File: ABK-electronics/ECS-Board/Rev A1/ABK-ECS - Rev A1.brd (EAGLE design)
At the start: 80 x 80 mm, 141 parts, among them J1 1241050-5, J2 USB3075-30-A, J3 22-27-2061-06, J4 22-05-7068-06, J5 22-05-7028-02, J6 22-05-7028-02, J7 22-05-7068-06, K3 G6K-2G-Y, SW1 B3FS-1015, SW2 B3FS-1015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

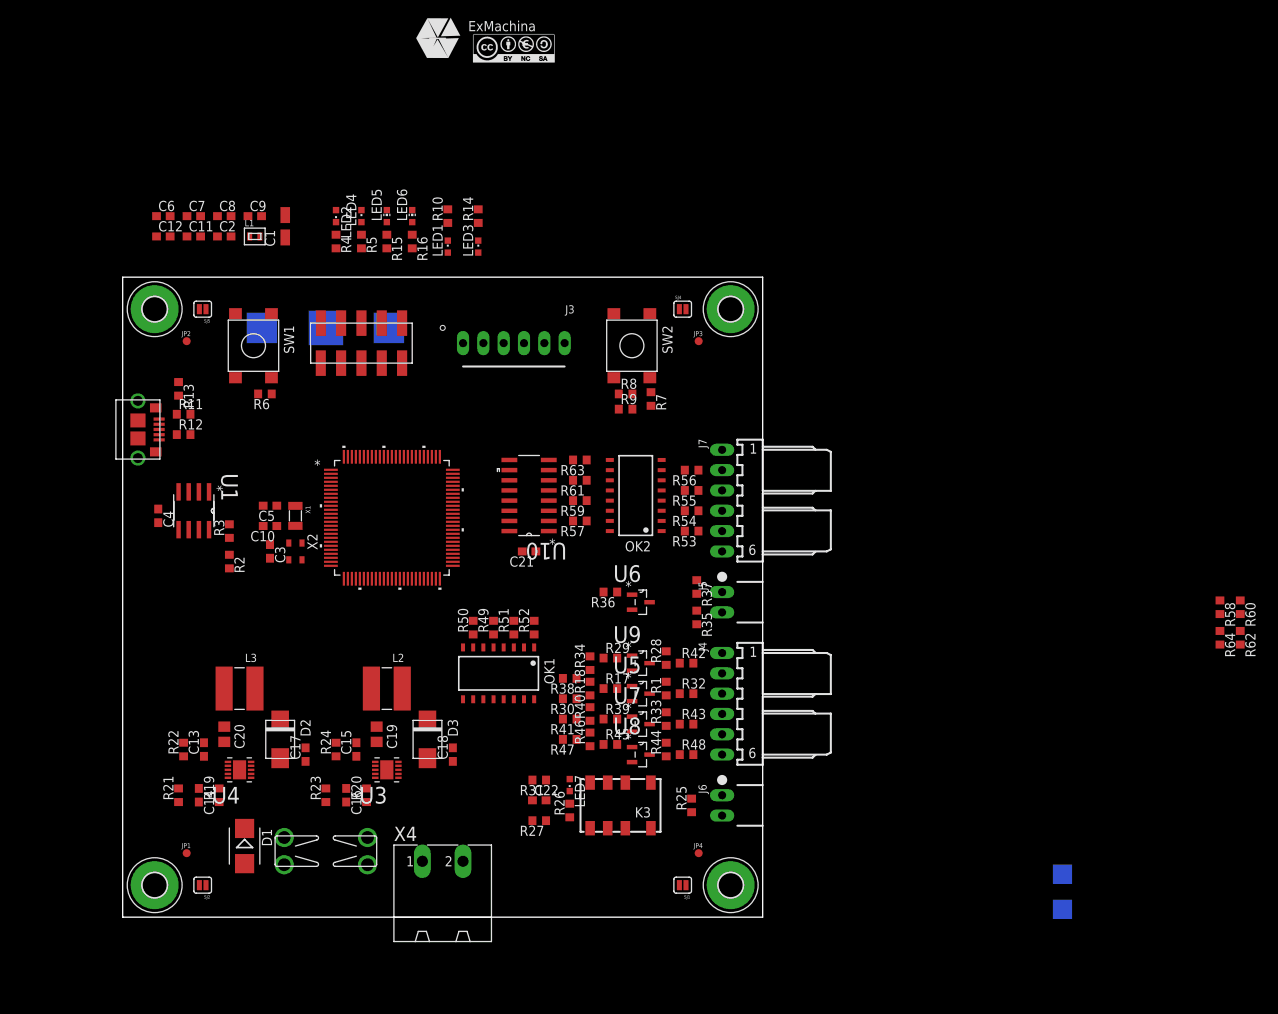
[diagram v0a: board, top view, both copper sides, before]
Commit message: Route the board and modify schematic
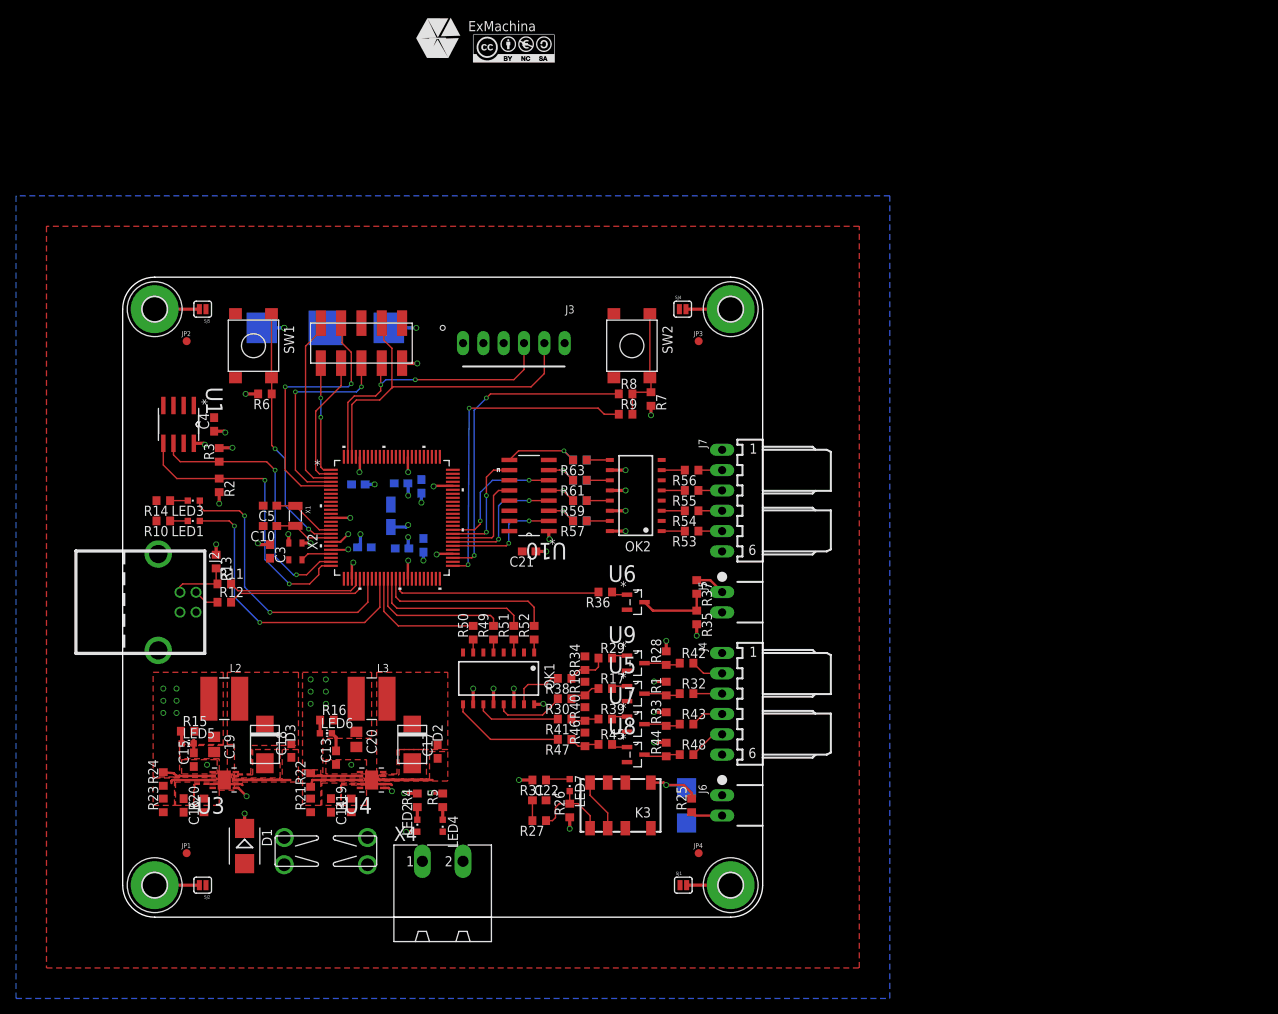
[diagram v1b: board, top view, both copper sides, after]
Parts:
- removed C9: 0.1uF, rcl:C0603
- removed L1: 0603PS-103KLB, coilcraft:0603
- J2: value USB3075-30-A -> USB-B-S-RA; device con-GlobalConnectorTechnology:USB_MICROB_SMT -> con-multicomp:USB-B-S-RA
- moved R62 84.9 mm to (57.1, 54.6), flipped to the bottom, turned to 180 degrees
- moved R60 83.6 mm to (57.1, 52.1), flipped to the bottom, turned to 180 degrees
- moved R64 83.0 mm to (57.1, 57.1), flipped to the bottom, turned to 180 degrees
- moved R58 80.7 mm to (57.1, 49.5), flipped to the bottom, turned to 180 degrees
- moved LED4 76.9 mm to (40.0, 11.4), turned to 180 degrees
- moved LED2 76.9 mm to (36.8, 11.4), turned to 0 degrees
- moved R4 70.6 mm to (36.8, 14.6), turned to 90 degrees
- moved R5 70.6 mm to (40.0, 14.6), turned to 90 degrees
- moved LED5 70.5 mm to (8.13, 21.7), turned to 270 degrees
- moved R15 66.1 mm to (8.13, 23.2), turned to 0 degrees
- moved LED6 65.5 mm to (25.4, 23.0), turned to 270 degrees
- moved R16 60.8 mm to (25.5, 24.6), turned to 0 degrees
- moved R14 53.1 mm to (5.08, 52.1), turned to 180 degrees
- moved R10 52.1 mm to (5.08, 49.5), turned to 180 degrees
- moved C7 50.2 mm to (37.6, 46.5), flipped to the bottom, turned to 90 degrees
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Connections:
- removed net AVDD: C9.1, L1.P$2, U2.10, U2.12
- removed net N$27: R36.2
- removed net N$58: U2.40
- new net 2: MP2.1, SJ5.2
- new net 3: MP3.1, SJ4.2
- new net 4: MP4.1, SJ1.2
- new net MOTOR_CONTROL_MCU: R36.2, U2.40
- new net VDDA: U2.10
- new net VREFP: U2.12
- net +3V3: no longer L1.P$1
- net 1: no longer MP2.1, MP3.1, MP4.1, SJ1.2, SJ4.2, SJ5.2
- net GND: now also J2.4, U1.7; no longer C9.2, J2.5
- net N$1: now also J2.3; no longer J2.2
- net N$2: now also J2.2; no longer J2.3
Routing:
- net VBAT+: track 0.00 -> 52.8 mm, vias 0 -> 4
- net +3V3: track 0.00 -> 50.2 mm, vias 0 -> 33
- net ISP_TXDO: track 0.00 -> 44.6 mm
- net BOOT_SELECT_P2_12: track 0.00 -> 40.6 mm, vias 0 -> 2
- net BOOT_SELECT_P2_10: track 0.00 -> 39.9 mm, vias 0 -> 2
- net EEPROM_SDA: track 0.00 -> 37.7 mm, vias 0 -> 2
- net LED_DEBUG: track 0.00 -> 37.3 mm, vias 0 -> 2
- net ISP_RXDO: track 0.00 -> 37.0 mm, vias 0 -> 2
- net USB_UP_LED: track 0.00 -> 35.9 mm, vias 0 -> 2
- net EEPROM_SCL: track 0.00 -> 34.4 mm, vias 0 -> 2
- net JTAG_TCK: track 0.00 -> 33.5 mm, vias 0 -> 2
- net !RESET: track 0.00 -> 31.8 mm, vias 0 -> 2
- net MOTOR_CONTROL_MCU: track 0.00 -> 26.5 mm
- net !JTAG_TRST: track 0.00 -> 26.3 mm, vias 0 -> 2
- net USB_V_BUS: track 0.00 -> 24.5 mm, vias 0 -> 1
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- added copper zone on layer 1, net +24V
- added copper zone on layer 3, net +24V
- added copper zone on layer 1, net +3V3
- added copper zone on layer 3, net +3V3
- added copper zone on layer 1, net +5V
- added copper zone on layer 3, net +5V
- added copper zone on layer 1, net GND
- added copper zone on layer 16, net GND
- added copper zone on layer 2, net GND
- added copper zone on layer 1, net N$10
- added copper zone on layer 1, net N$11
- added copper zone on layer 1, net N$12
- added copper zone on layer 1, net N$13
- added copper zone on layer 1, net N$14
- added copper zone on layer 1, net N$15
- added copper zone on layer 1, net N$16
- added copper zone on layer 1, net N$4
- added copper zone on layer 1, net N$6
- added copper zone on layer 1, net N$7
- added copper zone on layer 1, net N$8
- added copper zone on layer 1, net N$9
- added copper zone on layer 3, net VIN
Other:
- outline, holes or cut-outs redrawn
